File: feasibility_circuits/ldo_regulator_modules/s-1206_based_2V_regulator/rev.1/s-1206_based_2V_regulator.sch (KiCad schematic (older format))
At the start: 32 parts, among them J1 Jumper, J2 Jumper, J3 Jumper, J4 Jumper, J5 Jumper, J6 Jumper, P1 VIN, P10 TEST_VOUT_1_2, P11 TEST_VOUT_2_2, P12 TEST_VOUT_3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

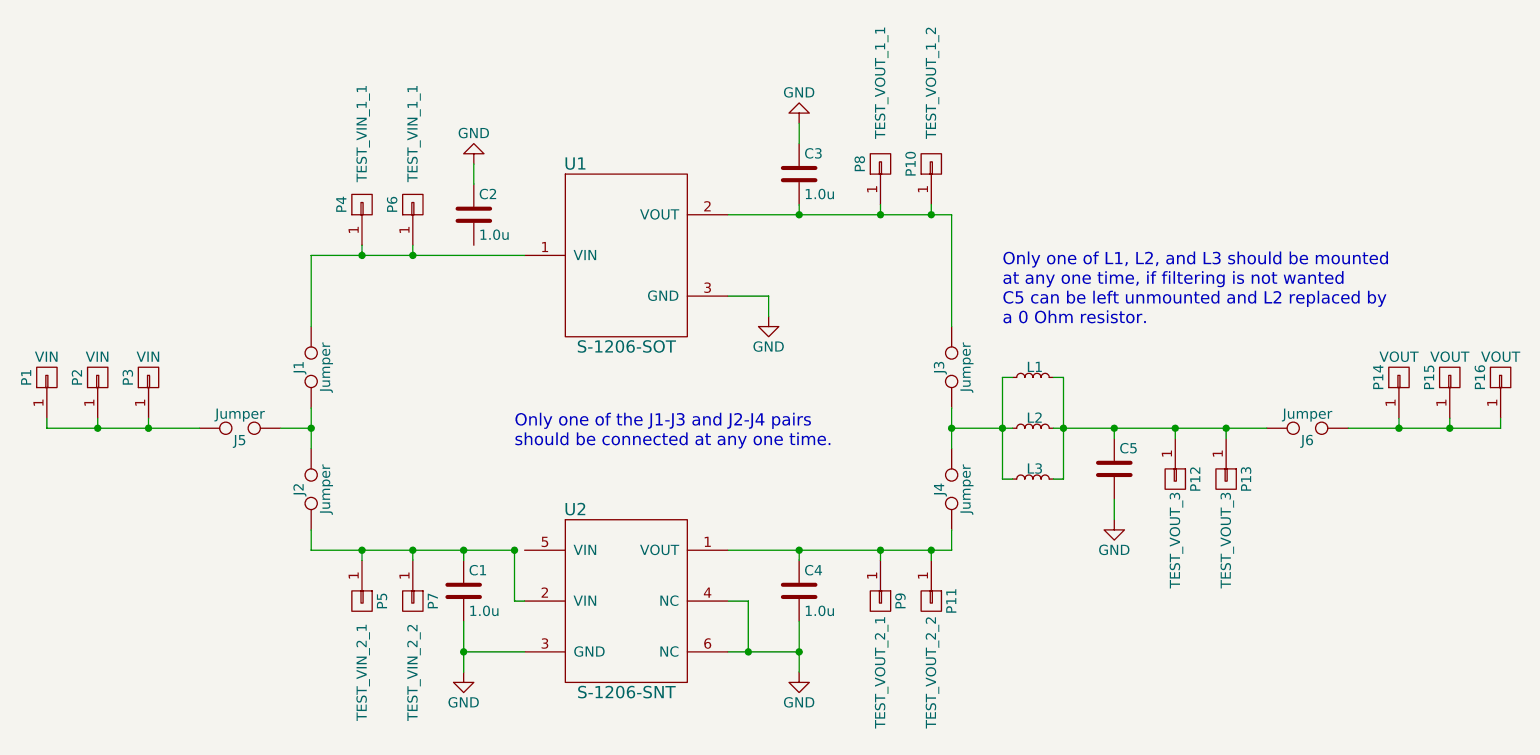
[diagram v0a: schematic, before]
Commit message: Completed initial draft of layout for S-1206 LDO prototype board
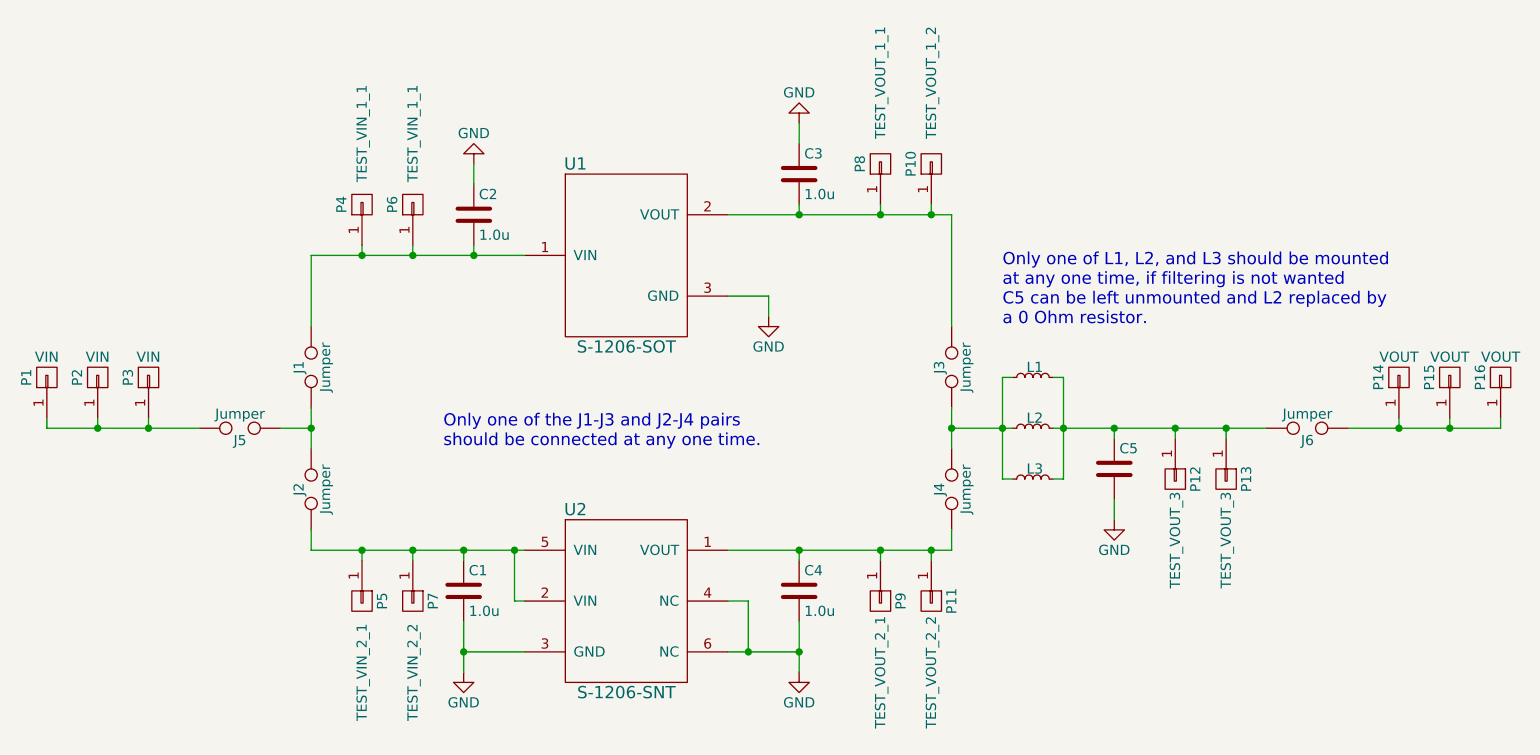
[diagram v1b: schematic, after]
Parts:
- U1: footprint (none) -> custom_amplifiers_smd:proto_amp-sii_s_1206_SOT_23
- U2: footprint (none) -> custom_amplifiers_smd:proto_amp-sii_s_1206_SNT_6A
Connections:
- net at C1.1, J2.1, P5.1 (P1)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: now also U2.5 (VIN)
- net at J1.2, P4.1 (P1), P6.1 (P1)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: now also C2.2
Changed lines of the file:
@@
 encoding utf-8
 Sheet 1 1
-Title ""
+Title "SII S-1206 LDO Prototype Board"
 Date ""
-Rev ""
-Comp ""
+Rev "A"
+Comp "Innovation Zed/Hotswap Norden AB"
 Comment1 ""
 Comment2 ""
@@
 F 0 "U2" H 5250 5050 60  0000 C CNN
 F 1 "S-1206-SNT" H 5500 4150 60  0000 C CNN
-F 2 "" H 5500 4500 60  0001 C CNN
+F 2 "custom_amplifiers_smd:proto_amp-sii_s_1206_SNT_6A" H 5500 4500 60  0001 C CNN
 F 3 "" H 5500 4500 60  0001 C CNN
 	1    5500 4600
@@
 F 0 "U1" H 5250 3350 60  0000 C CNN
 F 1 "S-1206-SOT" H 5500 2450 60  0000 C CNN
-F 2 "" H 5500 2800 60  0001 C CNN
+F 2 "custom_amplifiers_smd:proto_amp-sii_s_1206_SOT_23" H 5500 2800 60  0001 C CNN
 F 3 "" H 5500 2800 60  0001 C CNN
 	1    5500 2900
@@
 	0    1    1    0
 $EndComp
-Wire Wire Line
-	2900 3700 2900 3750
-Wire Wire Line
-	2650 3750 3400 3750
-Wire Wire Line
-	3150 3700 3150 3750
-Connection ~ 3150 3750
-Wire Wire Line
-	3800 3750 3950 3750
-Wire Wire Line
-	3950 4350 4950 4350
-Connection ~ 3950 3750
-Wire Wire Line
-	4950 4350 4950 4600
-Wire Wire Line
-	4950 4600 5000 4600
-Connection ~ 4950 4350
-Connection ~ 4700 4350
-Connection ~ 4450 4350
-Wire Wire Line
-	4450 4400 4450 4350
-Wire Wire Line
-	4700 4400 4700 4350
-Wire Wire Line
-	4700 4700 4700 4950
-Wire Wire Line
-	4700 4850 5000 4850
-Connection ~ 4700 4850
-Wire Wire Line
-	7100 3750 7400 3750
-Wire Wire Line
-	7350 3500 7350 4000
-Wire Wire Line
-	7350 3500 7400 3500
-Connection ~ 7350 3750
-Wire Wire Line
-	7350 4000 7400 4000
-Wire Wire Line
-	7900 3800 7900 3750
-Connection ~ 7900 3750
-Wire Wire Line
-	7650 4000 7600 4000
-Wire Wire Line
-	7650 3500 7650 4000
-Connection ~ 7650 3750
-Wire Wire Line
-	7600 3500 7650 3500
-Wire Wire Line
-	7900 4100 7900 4200
-Wire Wire Line
-	9050 3750 9800 3750
-Wire Wire Line
-	9800 3750 9800 3700
-Wire Wire Line
-	9550 3700 9550 3750
-Connection ~ 9550 3750
-Wire Wire Line
-	9300 3700 9300 3750
-Connection ~ 9300 3750
-Wire Wire Line
-	6350 2350 6350 2250
-Connection ~ 7100 3750
-Wire Wire Line
-	6350 4400 6350 4350
-Connection ~ 6350 4350
-Wire Wire Line
-	6750 4350 6750 4400
-Connection ~ 6750 4350
-Wire Wire Line
-	6000 4600 6100 4600
-Wire Wire Line
-	6100 4600 6100 4850
-Wire Wire Line
-	6350 4700 6350 4950
-Connection ~ 6350 4850
-Connection ~ 6100 4850
-$Comp
-L GND #PWR5
+$Comp
+L GND #PWR01
 U 1 1 5908D6B8
 P 6350 4950
-F 0 "#PWR5" H 6350 4700 50  0001 C CNN
+F 0 "#PWR01" H 6350 4700 50  0001 C CNN
 F 1 "GND" H 6350 4800 50  0000 C CNN
 F 2 "" H 6350 4950 50  0000 C CNN
@@
 $EndComp
 $Comp
-L GND #PWR1
+L GND #PWR02
 U 1 1 5908D764
 P 4700 4950
-F 0 "#PWR1" H 4700 4700 50  0001 C CNN
+F 0 "#PWR02" H 4700 4700 50  0001 C CNN
 F 1 "GND" H 4700 4800 50  0000 C CNN
 F 2 "" H 4700 4950 50  0000 C CNN
@@
 $EndComp
 $Comp
-L GND #PWR3
+L GND #PWR03
 U 1 1 5908D861
 P 6200 3200
-F 0 "#PWR3" H 6200 2950 50  0001 C CNN
+F 0 "#PWR03" H 6200 2950 50  0001 C CNN
 F 1 "GND" H 6200 3050 50  0000 C CNN
 F 2 "" H 6200 3200 50  0000 C CNN
@@
 $EndComp
 $Comp
-L GND #PWR6
+L GND #PWR04
 U 1 1 5908D8AE
 P 7900 4200
-F 0 "#PWR6" H 7900 3950 50  0001 C CNN
+F 0 "#PWR04" H 7900 3950 50  0001 C CNN
 F 1 "GND" H 7900 4050 50  0000 C CNN
 F 2 "" H 7900 4200 50  0000 C CNN
@@
 $EndComp
 $Comp
-L GND #PWR2
+L GND #PWR05
 U 1 1 5908DAB3
 P 4750 2450
-F 0 "#PWR2" H 4750 2200 50  0001 C CNN
+F 0 "#PWR05" H 4750 2200 50  0001 C CNN
 F 1 "GND" H 4750 2300 50  0000 C CNN
 F 2 "" H 4750 2450 50  0000 C CNN
@@
 	-1   0    0    1
 $EndComp
-Wire Wire Line
-	4750 2550 4750 2450
 $Comp
 L TEST J1
@@
 	0    -1   -1   0
 $EndComp
-Wire Wire Line
-	3950 3650 3950 3850
-Wire Wire Line
-	3950 3250 3950 2900
-Wire Wire Line
-	7100 3650 7100 3850
-Wire Wire Line
-	7100 2700 7100 3250
-Text Notes 4950 3850 0    60   ~ 0
+Text Notes 4600 3850 0    60   ~ 0
 Only one of the J1-J3 and J2-J4 pairs \nshould be connected at any one time.
 Text Notes 7350 3250 0    60   ~ 0
 Only one of L1, L2, and L3 should be mounted \nat any one time, if filtering is not wanted \nC5 can be left unmounted and L2 replaced by \na 0 Ohm resistor.
 $Comp
-L GND #PWR4
+L GND #PWR06
 U 1 1 590916B3
 P 6350 2250
-F 0 "#PWR4" H 6350 2000 50  0001 C CNN
+F 0 "#PWR06" H 6350 2000 50  0001 C CNN
 F 1 "GND" H 6350 2100 50  0000 C CNN
 F 2 "" H 6350 2250 50  0000 C CNN
@@
 	-1   0    0    1
 $EndComp
-Wire Wire Line
-	6000 4850 6350 4850
 $Comp
 L CONN_01X01 P4
@@
 	0    1    1    0
 $EndComp
-Wire Wire Line
-	6000 4350 7100 4350
-Wire Wire Line
-	7100 4350 7100 4250
-Wire Wire Line
-	7000 4400 7000 4350
-Connection ~ 7000 4350
-Wire Wire Line
-	3950 4350 3950 4250
-Wire Wire Line
-	4200 4400 4200 4350
-Connection ~ 4200 4350
-Wire Wire Line
-	3950 2900 5000 2900
-Wire Wire Line
-	4200 2850 4200 2900
-Connection ~ 4200 2900
-Wire Wire Line
-	4450 2850 4450 2900
-Connection ~ 4450 2900
-Wire Wire Line
-	6000 3100 6200 3100
-Wire Wire Line
-	6200 3100 6200 3200
-Wire Wire Line
-	6000 2700 7100 2700
-Wire Wire Line
-	6350 2650 6350 2700
-Connection ~ 6350 2700
-Wire Wire Line
-	6750 2650 6750 2700
-Connection ~ 6750 2700
-Wire Wire Line
-	7000 2650 7000 2700
-Connection ~ 7000 2700
 $Comp
 L CONN_01X01 P13
@@
 	0    1    1    0
 $EndComp
-Wire Wire Line
-	7600 3750 8650 3750
-Wire Wire Line
-	8200 3800 8200 3750
-Connection ~ 8200 3750
-Wire Wire Line
-	8450 3800 8450 3750
-Connection ~ 8450 3750
 $Comp
 L CONN_01X01 P1
@@
 $EndComp
 Wire Wire Line
+	2900 3700 2900 3750
+Wire Wire Line
+	2650 3750 3400 3750
+Wire Wire Line
+	3150 3700 3150 3750
+Connection ~ 3150 3750
+Wire Wire Line
+	3800 3750 3950 3750
+Wire Wire Line
+	3950 4350 5000 4350
+Connection ~ 3950 3750
+Wire Wire Line
+	4950 4350 4950 4600
+Wire Wire Line
+	4950 4600 5000 4600
+Connection ~ 4950 4350
+Connection ~ 4700 4350
+Connection ~ 4450 4350
+Wire Wire Line
+	4450 4400 4450 4350
+Wire Wire Line
+	4700 4400 4700 4350
+Wire Wire Line
+	4700 4700 4700 4950
+Connection ~ 4700 4850
+Wire Wire Line
+	7100 3750 7400 3750
+Wire Wire Line
+	7350 3500 7350 4000
+Wire Wire Line
+	7350 3500 7400 3500
+Connection ~ 7350 3750
+Wire Wire Line
+	7350 4000 7400 4000
+Wire Wire Line
+	7900 3800 7900 3750
+Connection ~ 7900 3750
+Wire Wire Line
+	7650 4000 7600 4000
+Wire Wire Line
+	7650 3500 7650 4000
+Connection ~ 7650 3750
+Wire Wire Line
+	7600 3500 7650 3500
+Wire Wire Line
+	7900 4100 7900 4200
+Wire Wire Line
+	9050 3750 9800 3750
+Wire Wire Line
+	9800 3750 9800 3700
+Wire Wire Line
+	9550 3700 9550 3750
+Connection ~ 9550 3750
+Wire Wire Line
+	9300 3700 9300 3750
+Connection ~ 9300 3750
+Wire Wire Line
+	6350 2350 6350 2250
+Connection ~ 7100 3750
+Wire Wire Line
+	6350 4400 6350 4350
+Connection ~ 6350 4350
+Wire Wire Line
+	6750 4350 6750 4400
+Connection ~ 6750 4350
+Wire Wire Line
+	6000 4600 6100 4600
+Wire Wire Line
+	6350 4700 6350 4950
+Connection ~ 6350 4850
+Wire Wire Line
+	4750 2550 4750 2450
+Wire Wire Line
+	3950 3650 3950 3850
+Wire Wire Line
+	3950 3250 3950 2900
+Wire Wire Line
+	7100 3650 7100 3850
+Wire Wire Line
+	7100 2700 7100 3250
+Wire Wire Line
+	6000 4350 7100 4350
+Wire Wire Line
+	7100 4350 7100 4250
+Wire Wire Line
+	7000 4400 7000 4350
+Connection ~ 7000 4350
+Wire Wire Line
+	3950 4350 3950 4250
+Wire Wire Line
+	4200 4400 4200 4350
+Connection ~ 4200 4350
+Wire Wire Line
+	3950 2900 5000 2900
+Wire Wire Line
+	4200 2850 4200 2900
+Connection ~ 4200 2900
+Wire Wire Line
+	4450 2850 4450 2900
+Connection ~ 4450 2900
+Wire Wire Line
+	6000 3100 6200 3100
+Wire Wire Line
+	6200 3100 6200 3200
+Wire Wire Line
+	6000 2700 7100 2700
+Wire Wire Line
+	6350 2650 6350 2700
+Connection ~ 6350 2700
+Wire Wire Line
+	6750 2650 6750 2700
+Connection ~ 6750 2700
+Wire Wire Line
+	7000 2650 7000 2700
+Connection ~ 7000 2700
+Wire Wire Line
+	7600 3750 8650 3750
+Wire Wire Line
+	8200 3800 8200 3750
+Connection ~ 8200 3750
+Wire Wire Line
+	8450 3800 8450 3750
+Connection ~ 8450 3750
+Wire Wire Line
 	2650 3700 2650 3750
 Connection ~ 2900 3750
+Wire Wire Line
+	4750 2850 4750 2900
+Connection ~ 4750 2900
+Wire Wire Line
+	6000 4850 6350 4850
+Wire Wire Line
+	4700 4850 5000 4850
+Wire Wire Line
+	6100 4600 6100 4850
+Connection ~ 6100 4850
 $EndSCHEMATC
